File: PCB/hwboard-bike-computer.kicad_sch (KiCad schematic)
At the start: 0 parts

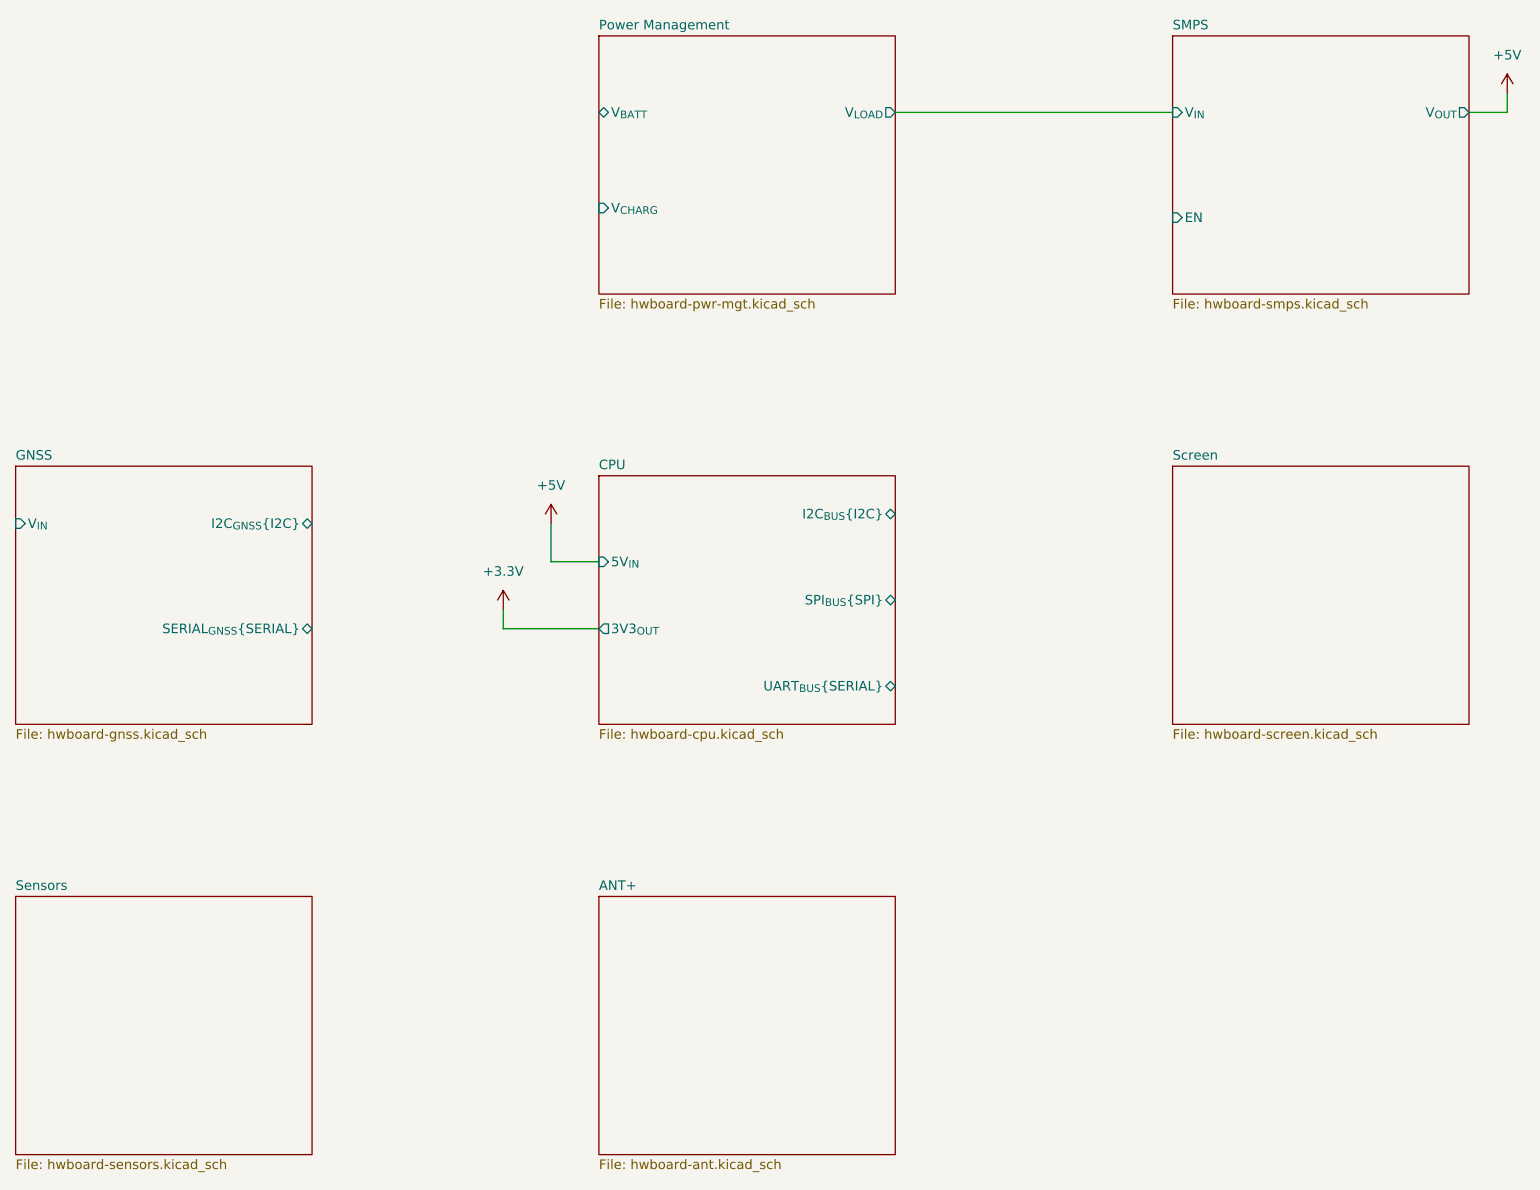
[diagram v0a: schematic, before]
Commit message: add sensors components
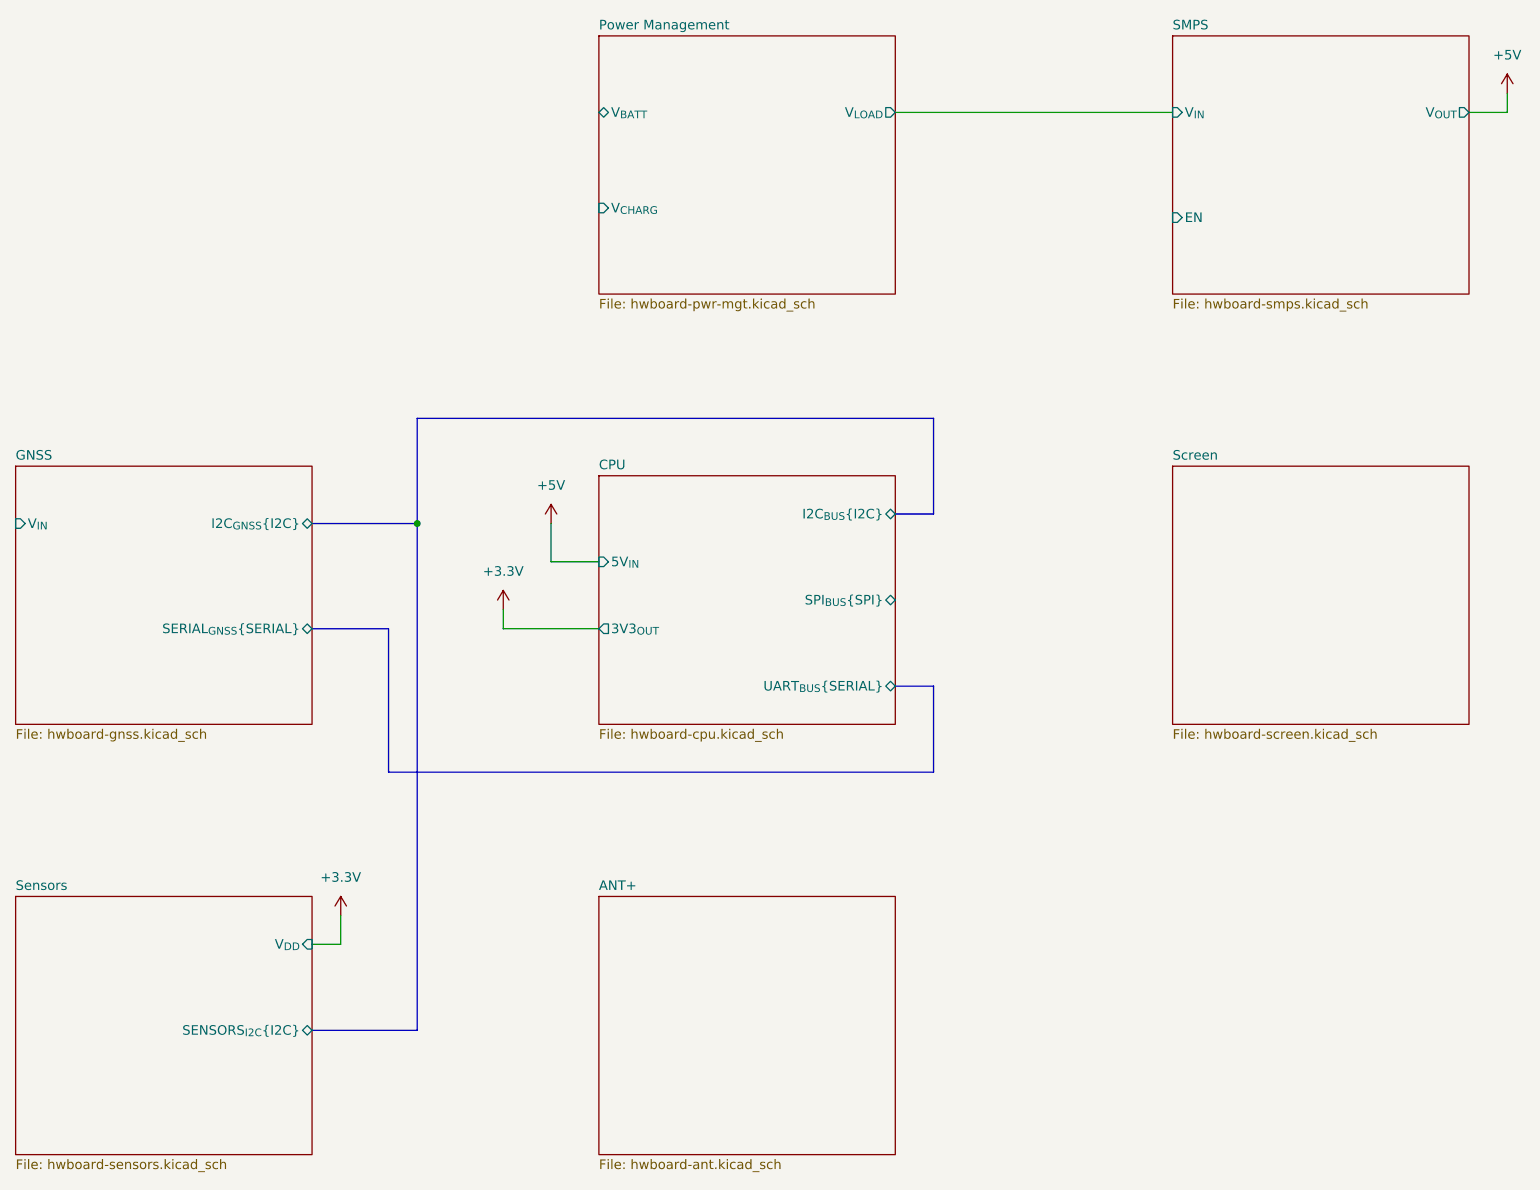
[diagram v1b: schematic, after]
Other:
- sheet Sensors ports: added SENSORS_{I2C}{I2C}, V_{DD}; removed none
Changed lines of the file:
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@@
 		(members "TX" "RX")
 	)
+	(junction
+		(at 105.41 92.71)
+		(diameter 0)
+		(color 0 0 0 0)
+	)
+	(bus
+		(pts
+			(xy 101.6 125.73) (xy 173.99 125.73)
+		)
+		(stroke
+			(width 0)
+			(type default)
+		)
+	)
+	(bus
+		(pts
+			(xy 173.99 125.73) (xy 173.99 114.3)
+		)
+		(stroke
+			(width 0)
+			(type default)
+		)
+	)
+	(wire
+		(pts
+			(xy 95.25 144.78) (xy 95.25 148.59)
+		)
+		(stroke
+			(width 0)
+			(type default)
+		)
+	)
+	(bus
+		(pts
+			(xy 105.41 160.02) (xy 105.41 92.71)
+		)
+		(stroke
+			(width 0)
+			(type default)
+		)
+	)
+	(bus
+		(pts
+			(xy 168.91 91.44) (xy 173.99 91.44)
+		)
+		(stroke
+			(width 0)
+			(type default)
+		)
+	)
+	(wire
+		(pts
+			(xy 95.25 148.59) (xy 91.44 148.59)
+		)
+		(stroke
+			(width 0)
+			(type default)
+		)
+	)
+	(bus
+		(pts
+			(xy 105.41 92.71) (xy 91.44 92.71)
+		)
+		(stroke
+			(width 0)
+			(type default)
+		)
+	)
+	(bus
+		(pts
+			(xy 105.41 78.74) (xy 105.41 92.71)
+		)
+		(stroke
+			(width 0)
+			(type default)
+		)
+	)
 	(wire
 		(pts
@@
 		)
 	)
+	(bus
+		(pts
+			(xy 173.99 91.44) (xy 173.99 78.74)
+		)
+		(stroke
+			(width 0)
+			(type default)
+		)
+	)
+	(bus
+		(pts
+			(xy 91.44 160.02) (xy 105.41 160.02)
+		)
+		(stroke
+			(width 0)
+			(type default)
+		)
+	)
 	(wire
 		(pts
@@
 		)
 	)
+	(bus
+		(pts
+			(xy 173.99 114.3) (xy 168.91 114.3)
+		)
+		(stroke
+			(width 0)
+			(type default)
+		)
+	)
+	(bus
+		(pts
+			(xy 173.99 78.74) (xy 105.41 78.74)
+		)
+		(stroke
+			(width 0)
+			(type default)
+		)
+	)
 	(wire
 		(pts
@@
 		)
 	)
+	(bus
+		(pts
+			(xy 91.44 106.68) (xy 101.6 106.68)
+		)
+		(stroke
+			(width 0)
+			(type default)
+		)
+	)
+	(bus
+		(pts
+			(xy 101.6 106.68) (xy 101.6 125.73)
+		)
+		(stroke
+			(width 0)
+			(type default)
+		)
+	)
 	(wire
 		(pts
@@
 			(width 0)
 			(type default)
+		)
+	)
+	(symbol
+		(lib_id "power:+3.3V")
+		(at 95.25 144.78 0)
+		(unit 1)
+		(exclude_from_sim no)
+		(in_bom yes)
+		(on_board yes)
+		(dnp no)
+		(fields_autoplaced yes)
+		(property "Reference" "#PWR036"
+			(at 95.25 148.59 0)
+			(effects
+				(font
+					(size 1.27 1.27)
+				)
+				(hide yes)
+			)
+		)
+		(property "Value" "+3.3V"
+			(at 95.25 139.7 0)
+			(effects
+				(font
+					(size 1.27 1.27)
+				)
+			)
+		)
+		(property "Footprint" ""
+			(at 95.25 144.78 0)
+			(effects
+				(font
+					(size 1.27 1.27)
+				)
+				(hide yes)
+			)
+		)
+		(property "Datasheet" ""
+			(at 95.25 144.78 0)
+			(effects
+				(font
+					(size 1.27 1.27)
+				)
+				(hide yes)
+			)
+		)
+		(property "Description" "Power symbol creates a global label with name \"+3.3V\""
+			(at 95.25 144.78 0)
+			(effects
+				(font
+					(size 1.27 1.27)
+				)
+				(hide yes)
+			)
+		)
+		(pin "1"
+		)
+		(instances
+			(project "hwboard-bike-computer"
+				(path "/8c0f76b9-ee42-4bcf-bb95-09772e367402"
+					(reference "#PWR036")
+					(unit 1)
+				)
+			)
 		)
 	)
@@
 			)
 		)
+		(pin "SENSORS_{I2C}{I2C}" bidirectional
+			(at 91.44 160.02 0)
+			(effects
+				(font
+					(size 1.27 1.27)
+				)
+				(justify right)
+			)
+		)
+		(pin "V_{DD}" input
+			(at 91.44 148.59 0)
+			(effects
+				(font
+					(size 1.27 1.27)
+				)
+				(justify right)
+			)
+		)

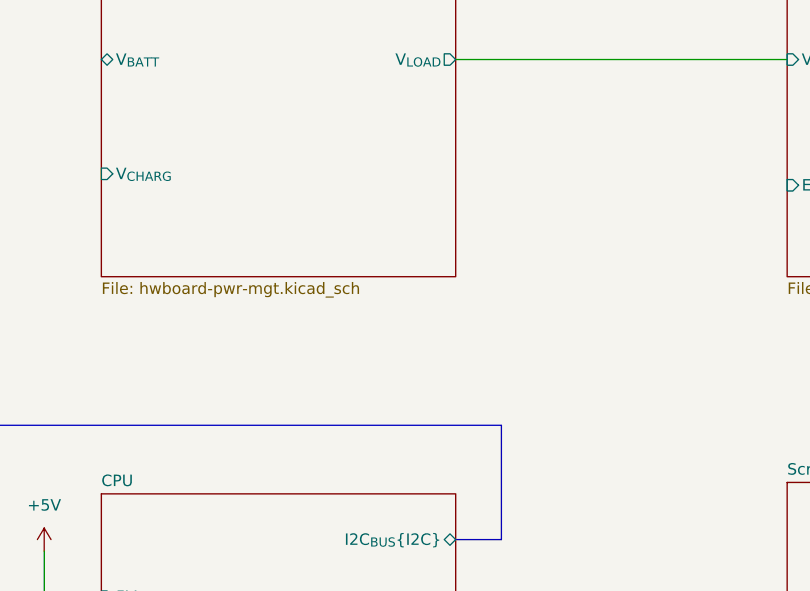
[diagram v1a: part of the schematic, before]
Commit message: add resistive touch IC
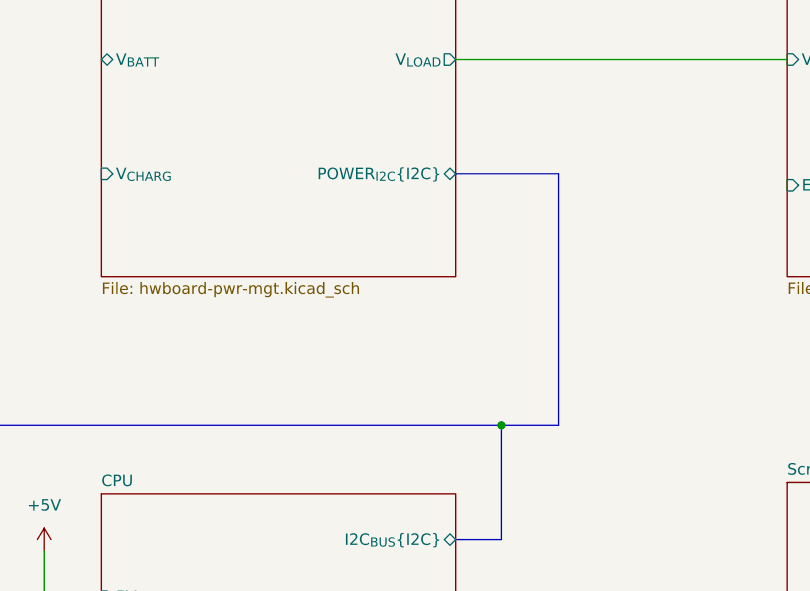
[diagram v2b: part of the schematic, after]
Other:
- sheet Power Management ports: added POWER_{I2C}{I2C}; removed none
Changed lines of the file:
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@@
 		(color 0 0 0 0)
 	)
+	(junction
+		(at 173.99 78.74)
+		(diameter 0)
+		(color 0 0 0 0)
+	)
 	(bus
 		(pts
@@
 		)
 	)
+	(bus
+		(pts
+			(xy 180.34 78.74) (xy 173.99 78.74)
+		)
+		(stroke
+			(width 0)
+			(type default)
+		)
+	)
 	(wire
 		(pts
@@
 	(bus
 		(pts
+			(xy 180.34 50.8) (xy 180.34 78.74)
+		)
+		(stroke
+			(width 0)
+			(type default)
+		)
+	)
+	(bus
+		(pts
 			(xy 91.44 160.02) (xy 105.41 160.02)
+		)
+		(stroke
+			(width 0)
+			(type default)
+		)
+	)
+	(bus
+		(pts
+			(xy 168.91 50.8) (xy 180.34 50.8)
 		)
 		(stroke
@@
 			)
 		)
+		(pin "POWER_{I2C}{I2C}" bidirectional
+			(at 168.91 50.8 0)
+			(effects
+				(font
+					(size 1.27 1.27)
+				)
+				(justify right)
+			)
+		)

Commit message: change filname
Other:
- sheet ANT+ renamed BLE + ANT+
- sheet BLE + ANT+: file hwboard-ant.kicad_sch -> hwboard-ble-ant.kicad_sch
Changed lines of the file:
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@@
 			(color 0 0 0 0)
 		)
-		(property "Sheetname" "ANT+"
+		(property "Sheetname" "BLE + ANT+"
 			(at 129.54 141.5284 0)
 			(show_name no)
@@
 			)
 		)
-		(property "Sheetfile" "hwboard-ant.kicad_sch"
+		(property "Sheetfile" "hwboard-ble-ant.kicad_sch"
 			(at 129.54 177.1146 0)
 			(show_name no)
